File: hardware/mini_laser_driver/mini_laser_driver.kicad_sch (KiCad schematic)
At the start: 48 parts, among them J1 Conn_01x02, J2 Conn_01x02, J3 Conn_01x02, J4 Conn_01x02, J5 Conn_01x02, J6 Conn_01x02, J7 Conn_01x02, Q1 BD139, Q2 BD139, Q3 BD139, U1 LM324, U2 R-78B3.3-2.0, U3 R-78B7.2-2.0

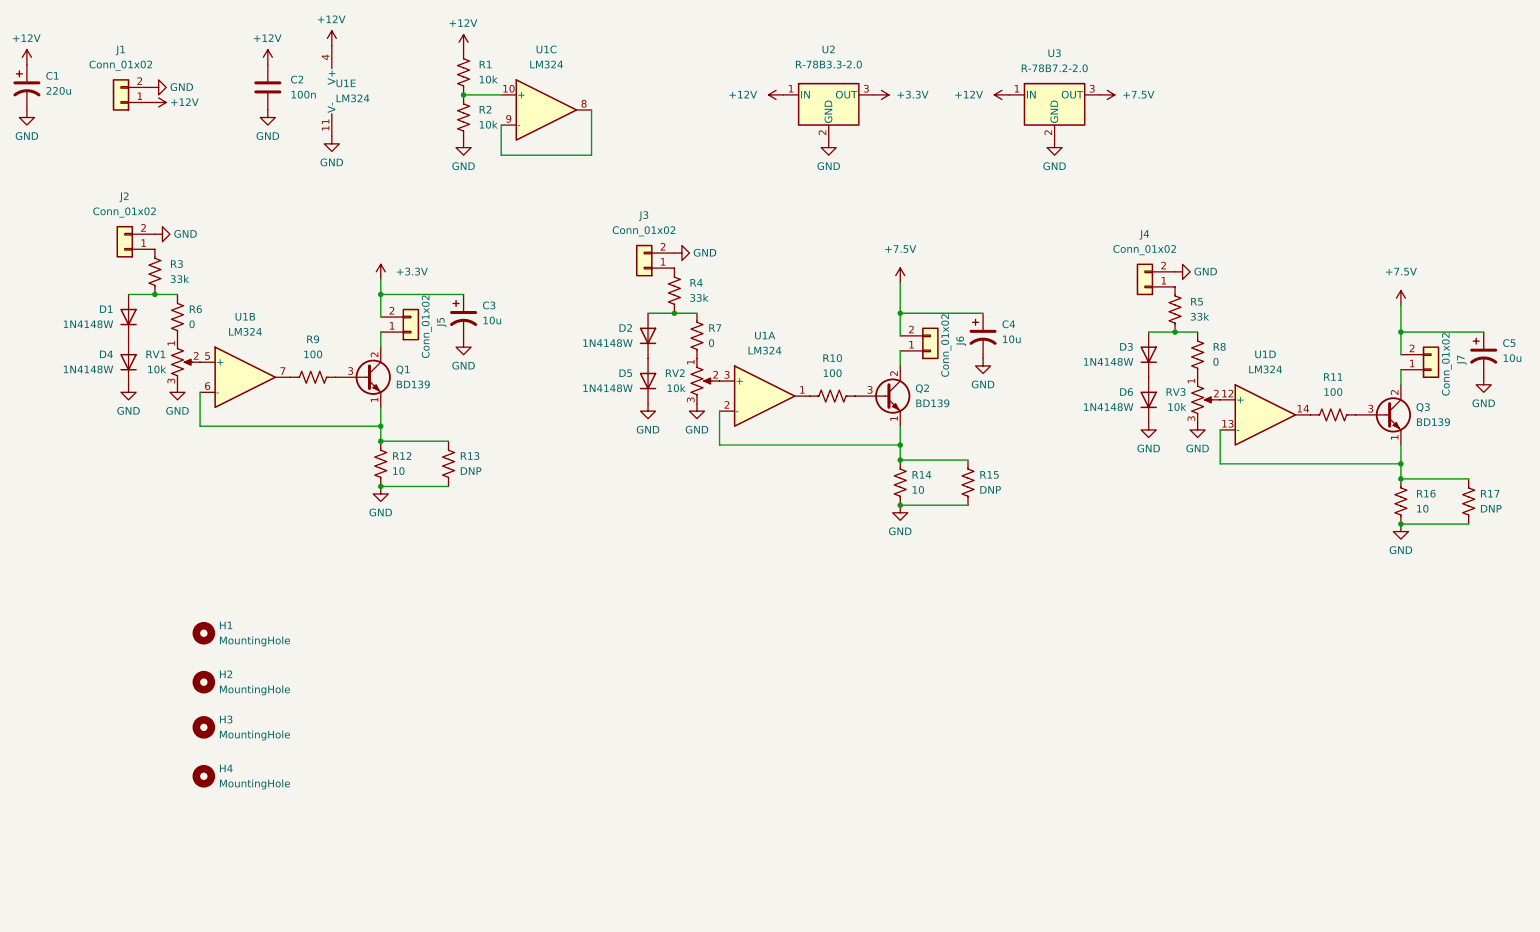
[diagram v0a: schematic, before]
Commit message: Improved laser driver design
The laser driver now allows you to switch between two different brightnesses with an external switch
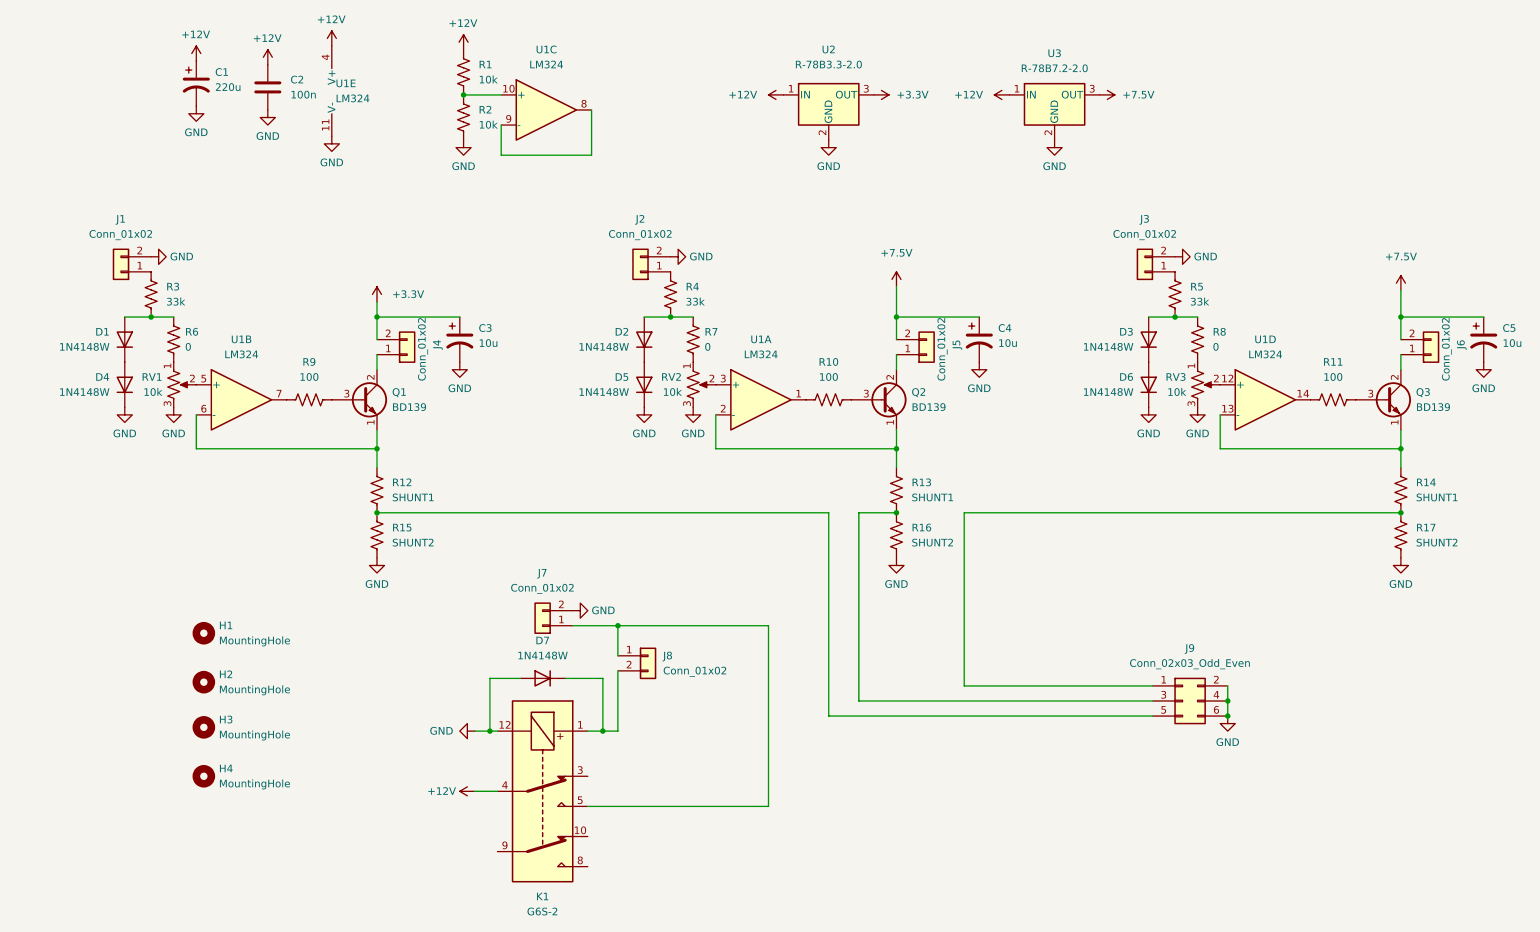
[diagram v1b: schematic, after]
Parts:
- removed R12, R14: 10, Resistor_SMD:R_1206_3216Metric, symbol Device:R_US
- added D7: 1N4148W, Diode_SMD:D_SOD-123, symbol Diode:1N4148W
- added J8: Conn_01x02, Connector_PinHeader_2.54mm:PinHeader_1x02_P2.54mm_Vertical, symbol Connector_Generic:Conn_01x02
- added J9: Conn_02x03_Odd_Even, Connector_PinHeader_2.54mm:PinHeader_2x03_P2.54mm_Vertical, symbol Connector_Generic:Conn_02x03_Odd_Even
- added K1: G6S-2, Relay_THT:Relay_DPDT_Omron_G6S-2, symbol Relay:G6S-2
- added R15, R17: SHUNT2, Resistor_THT:R_Axial_DIN0204_L3.6mm_D1.6mm_P1.90mm_Vertical, symbol Device:R_US
- R12: renamed from R13; value DNP -> SHUNT1
- R13: renamed from R15; value DNP -> SHUNT1
- R14: renamed from R17; value DNP -> SHUNT1
- R16: value 10 -> SHUNT2; footprint Resistor_SMD:R_1206_3216Metric -> Resistor_THT:R_Axial_DIN0204_L3.6mm_D1.6mm_P1.90mm_Vertical
- renumbered J2 to J1, J3 to J2, J4 to J3, J5 to J4, J6 to J5, J7 to J6, J1 to J7
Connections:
- net +12V: now also K1.4; no longer J7.1 (Pin_1)
- net GND: now also D7.2 (A), J9.2 (Pin_2), J9.4 (Pin_4), J9.6 (Pin_6), K1.12, R15.2, R17.2; no longer R12.2, R13.2, R14.2
- net at Q3.1 (E), R14.1, U1.13 (-): no longer R16.1
- new net: J9.5 (Pin_5), R12.2, R15.1
- new net: J7.1 (Pin_1), J8.1 (Pin_1), K1.5
- new net: D7.1 (K), J8.2 (Pin_2), K1.1
- new net: J9.3 (Pin_3), R13.2, R16.1
- new net: J9.1 (Pin_1), R14.2, R17.1
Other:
- moved on the sheet: C1, C3, C4, C5, D1, D2, D3, D4, D5, D6, J1, J2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
